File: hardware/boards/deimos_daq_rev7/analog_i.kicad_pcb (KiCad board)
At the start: 4 copper layers, 223 x 95 mm, 568 parts, among them IC10001 TPS560430XDBVR, IC11001 TPS560430XDBVR, IC13001 INA826AIDR, IC13002 TLV333IDBVR, IC13003 TLV333IDBVR, IC14001 TPS560430XDBVR, IC15001 INA826AIDR, IC17001 INA826AIDR, IC17002 TLV333IDBVR, IC17003 TLV333IDBVR, IC17004 BD42540FJ-CE2, IC20001 BD42540FJ-CE2, IC24001 BD42540FJ-CE2, IC28001 BD42540FJ-CE2, IC3002 BD42540FJ-CE2, IC36001 INA826AIDR, IC38001 INA826AIDR, IC4001 INA826AIDR, IC4002 TLV333IDBVR, IC4003 TLV333IDBVR, IC5001 INA826AIDR, IC5002 TLV333IDBVR, IC5003 TLV333IDBVR, IC5004 REF35102QDBVR, IC53001 INA826AIDR, IC54001 INA826AIDR, IC6001 STM32H743ZIT6, IC8001 INA826AIDR, IC9001 INA826AIDR, J13001 RCH_RC01133, J15001 AM-K-PCB, J3001 WJ15EDGRM-3.81-12P, J3002 WJ15EDGRM-3.81-12P, J3003 WJ15EDGRM-3.81-12P, J3004 WJ15EDGRM-3.81-12P, J3005 WJ15EDGRM-3.81-12P, J3006 WJ15EDGRM-3.81-12P, J3007 XG4C-2631, J6001 Conn_02x07_Odd_Even, J8001 Barrel_Jack PJ-202BH, J9001 AM-K-PCB, Q15001 MMBFJ113, Q15002 MMBFJ113, Q17001 MMBFJ113, Q17002 MMBFJ113, Q19001 MMBFJ113, Q19002 MMBFJ113, Q21001 MMBFJ113, Q21002 MMBFJ113, Q24001 MMBFJ113, Q24002 MMBFJ113, Q27001 MMBFJ113, Q27002 MMBFJ113, Q29001 MMBFJ113, Q29002 MMBFJ113, Q31001 MMBFJ113, Q31002 MMBFJ113, Q33001 MMBFJ113, Q33002 MMBFJ113, Q35001 MMBFJ113, Q35002 MMBFJ113, Q37001 MMBFJ113, Q37002 MMBFJ113, Q39001 MMBFJ113, Q39002 MMBFJ113, Q41001 MMBFJ113, Q41002 MMBFJ113, Q43001 MMBFJ113, Q43002 MMBFJ113, Q45001 MMBFJ113, Q45002 MMBFJ113, Q47001 MMBFJ113, Q47002 MMBFJ113, T7001 H1102NLT, U13001 NTJD4001NT1G, U15001 OPA196xDBV, U17001 NTJD4001NT1G, U17002 OPA196xDBV, U19001 OPA196xDBV, U21001 OPA196xDBV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

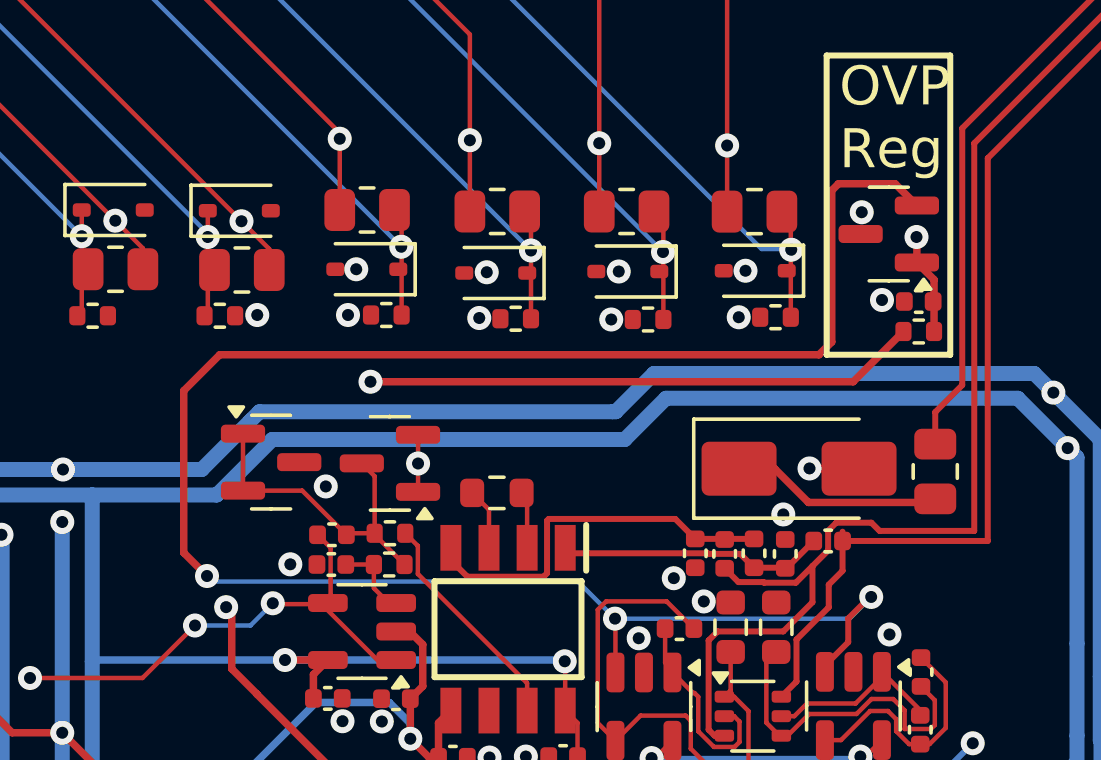
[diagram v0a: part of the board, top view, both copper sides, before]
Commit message: Deimos DAQ Rev 7.0.1 (#57)
## 2026-07-19 0.18.1

* Rev7 hardware
    * Finish pcb layout updates & re-generate fab files
    * Update enclosure graphics
* Rev7 firmware
    * Move `sample()` function with DSP pipeline into ITCM memory
    * Move `Net::poll` function with bulk of networking logic into ITCM
* This prevents them from being ejected from cache, or taking up space
in cache
* This should allow all remaining Operating-state code to remain in L1
cache (16kB)
* deimos
    * Update an example and reqwest dep
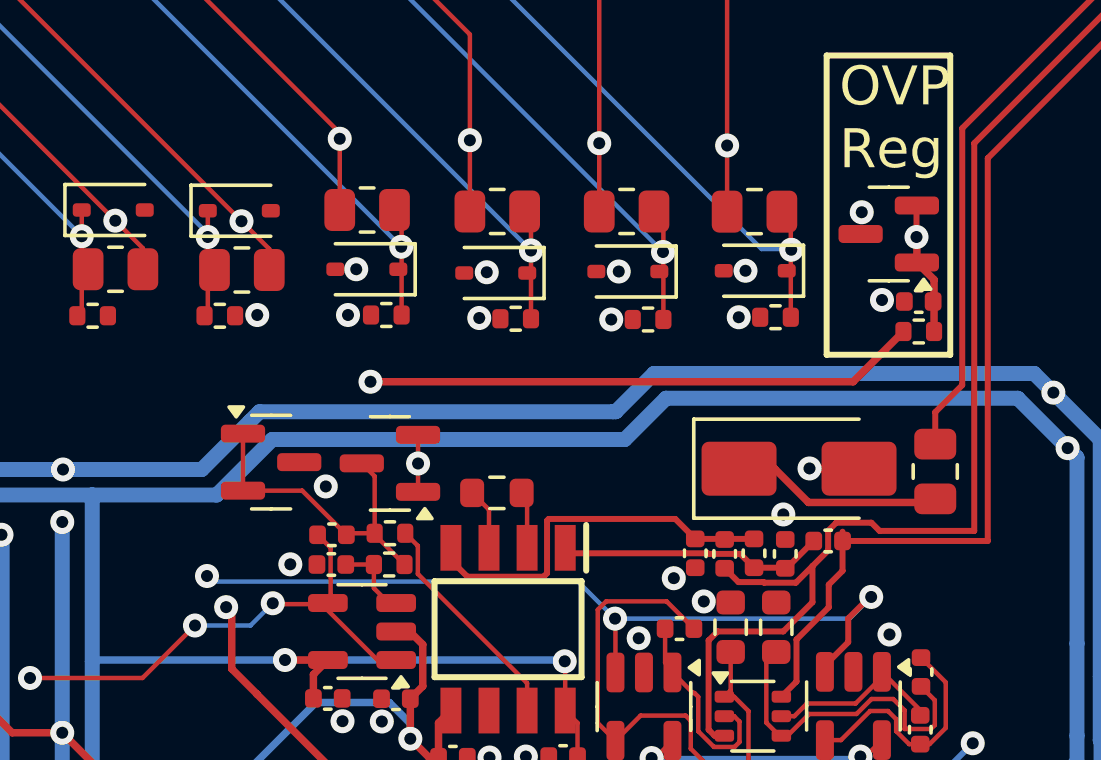
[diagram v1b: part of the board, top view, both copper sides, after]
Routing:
- net +2V5: track 331.6 -> 294.5 mm
- net 2V5_OVP: track 291.8 -> 292.9 mm
